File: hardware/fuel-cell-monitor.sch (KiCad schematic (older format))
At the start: 6 parts

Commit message: Upgraded version
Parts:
- added D?: Indicator, symbol LED
- added R?: 1k, symbol R
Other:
- moved on the sheet: SW?
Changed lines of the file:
@@
 LIBS:valves
 LIBS:arduino
+LIBS:fuel-cell-monitor-cache
 EELAYER 25 0
 EELAYER END
@@
 L SW_PUSH SW?
 U 1 1 582C96D8
-P 5300 3250
-F 0 "SW?" H 5450 3360 50  0000 C CNN
-F 1 "Write_control" H 5300 3170 50  0000 C CNN
-F 2 "" H 5300 3250 50  0000 C CNN
-F 3 "" H 5300 3250 50  0000 C CNN
-	1    5300 3250
+P 5250 3250
+F 0 "SW?" H 5400 3360 50  0000 C CNN
+F 1 "Write_control" H 5250 3170 50  0000 C CNN
+F 2 "" H 5250 3250 50  0000 C CNN
+F 3 "" H 5250 3250 50  0000 C CNN
+	1    5250 3250
 	0    1    1    0
 $EndComp
@@
 L GND #PWR?
 U 1 1 582C975D
-P 5300 3550
-F 0 "#PWR?" H 5300 3300 50  0001 C CNN
-F 1 "GND" H 5300 3400 50  0000 C CNN
-F 2 "" H 5300 3550 50  0000 C CNN
-F 3 "" H 5300 3550 50  0000 C CNN
-	1    5300 3550
+P 5250 3550
+F 0 "#PWR?" H 5250 3300 50  0001 C CNN
+F 1 "GND" H 5250 3400 50  0000 C CNN
+F 2 "" H 5250 3550 50  0000 C CNN
+F 3 "" H 5250 3550 50  0000 C CNN
+	1    5250 3550
 	1    0    0    -1
 $EndComp
 Wire Wire Line
-	5300 2950 4550 2950
+	5250 2950 4550 2950
+$Comp
+L LED D?
+U 1 1 582DD429
+P 5050 2650
+F 0 "D?" H 5050 2750 50  0000 C CNN
+F 1 "Indicator" H 5050 2550 50  0000 C CNN
+F 2 "" H 5050 2650 50  0000 C CNN
+F 3 "" H 5050 2650 50  0000 C CNN
+	1    5050 2650
+	-1   0    0    1
+$EndComp
+$Comp
+L R R?
+U 1 1 582DD478
+P 4700 2650
+F 0 "R?" V 4780 2650 50  0000 C CNN
+F 1 "1k" V 4700 2650 50  0000 C CNN
+F 2 "" V 4630 2650 50  0000 C CNN
+F 3 "" H 4700 2650 50  0000 C CNN
+	1    4700 2650
+	0    1    1    0
+$EndComp
+$Comp
+L GND #PWR?
+U 1 1 582DD4F9
+P 5250 2650
+F 0 "#PWR?" H 5250 2400 50  0001 C CNN
+F 1 "GND" H 5250 2500 50  0000 C CNN
+F 2 "" H 5250 2650 50  0000 C CNN
+F 3 "" H 5250 2650 50  0000 C CNN
+	1    5250 2650
+	1    0    0    -1
+$EndComp
 $EndSCHEMATC

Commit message: Add multiple things to schematic
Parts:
- removed R?: 470, symbol R
- removed U?: arduino_mini, DIL20, symbol arduino_mini
- added ARDUINO?: ARDUINO_NANO, symbol ARDUINO_NANO
- added D?: LED, symbol LED
- added D?: D_Schottky, symbol D_Schottky
- added M?: Solution pump, symbol DC_motor
- added M?: Air pump, symbol DC_motor
- added P?: Sense check, symbol CONN_01X02
- added P?: Light level sensor, symbol CONN_01X03
- added P?: Opacity sensor, symbol CONN_01X03
- added Q?: TEPT5600, symbol OPTO_NPN
- added Q?: TEPT5700, symbol OPTO_NPN
- added Q?: Q_NMOS_GDS, symbol Q_NMOS_GDS
- added R?: 10 k, symbol RVAR
- added R?: 1 k, symbol RVAR
- added R? (x2): 1 k, symbol R
- added R? (x2): 100, symbol R
- added R?: 1 M, symbol R
- added U?: LM35, symbol LM35
- P?: value Power_in -> Power in
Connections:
- net labels added: +12V, +5V
- wire segments 7 -> 33
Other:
- note added: "Light level sensor\n"
- note added: "Opacity sensor"
- moved on the sheet: D?, P?, R?, SW?

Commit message: Add missing parts to schematics
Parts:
- removed D?: Indicator, symbol LED
- removed D?: LED, symbol LED
- removed P?: Light level sensor, symbol CONN_01X03
- removed P?: Opacity sensor, symbol CONN_01X03
- removed Q?: TEPT5600, symbol OPTO_NPN
- removed Q?: TEPT5700, symbol OPTO_NPN
- removed R?: 1k, symbol R
- removed R? (x2): 1 k, symbol R
- removed R?: 100, symbol R
- added D?: Indicator, symbol LED
- added DS?: NHD-12232AZ, NHD-12232AZ, symbol NHD-12232AZ
- added R?: R, symbol R
- added RV?: 10 kA, symbol POT
- added S?: Light_level_sensor, symbol Light_level_sensor
- added S?: Opacity_sensor, symbol Opacity_sensor
- U?: value LM35 -> Temperature sensor
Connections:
- wire segments 33 -> 72
- no-connect marks 0 -> 6
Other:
- note removed: "Light level sensor\n"
- note removed: "Opacity sensor"
- moved on the sheet: ARDUINO?, D?, M?, P?, Q?, R?, SW?, U?

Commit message: Fix problems found with KiCad electrical rules check
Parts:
- gave numbers to parts that had none: 21
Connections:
- net +12V: now also ARDUINO1.30 (VIN), M2.2, P1.1 (P1)
- net at Q1.1 (G), R2.2: now also R1.1
- no-connect marks 6 -> 7
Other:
- moved on the sheet: P1, R1, R2

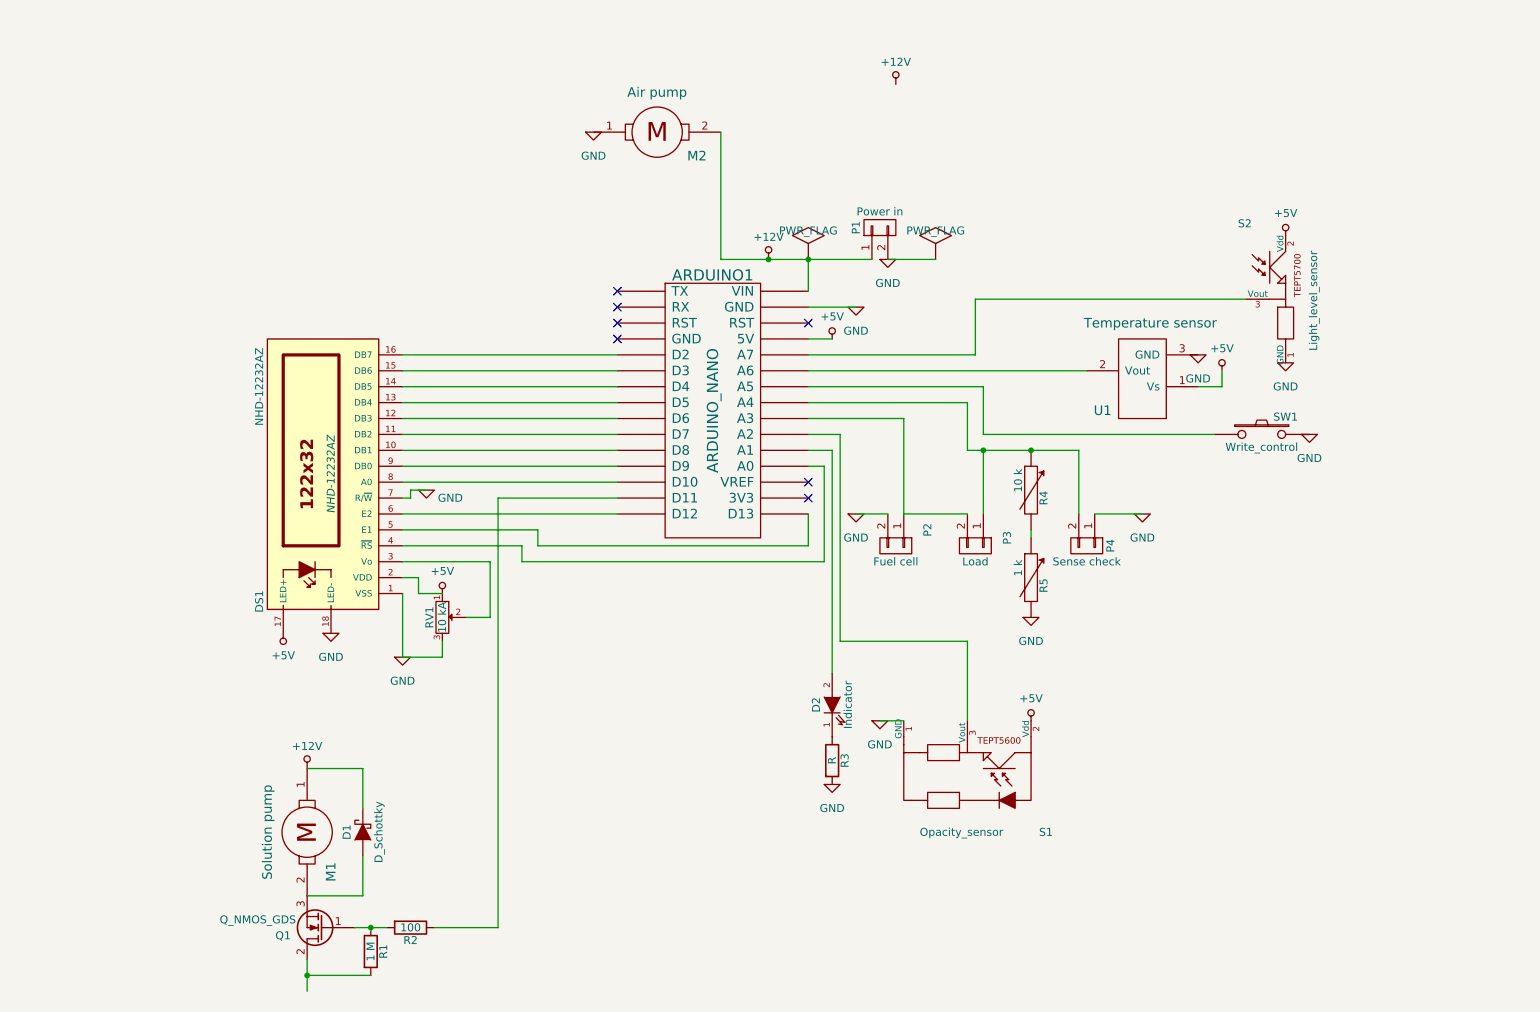
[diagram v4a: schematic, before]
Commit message: Fix remaining small things with the printed circuit board
This included making the default trace 0.40 mm wide just be sure
and fixing trimmer and potetiometer footprints.
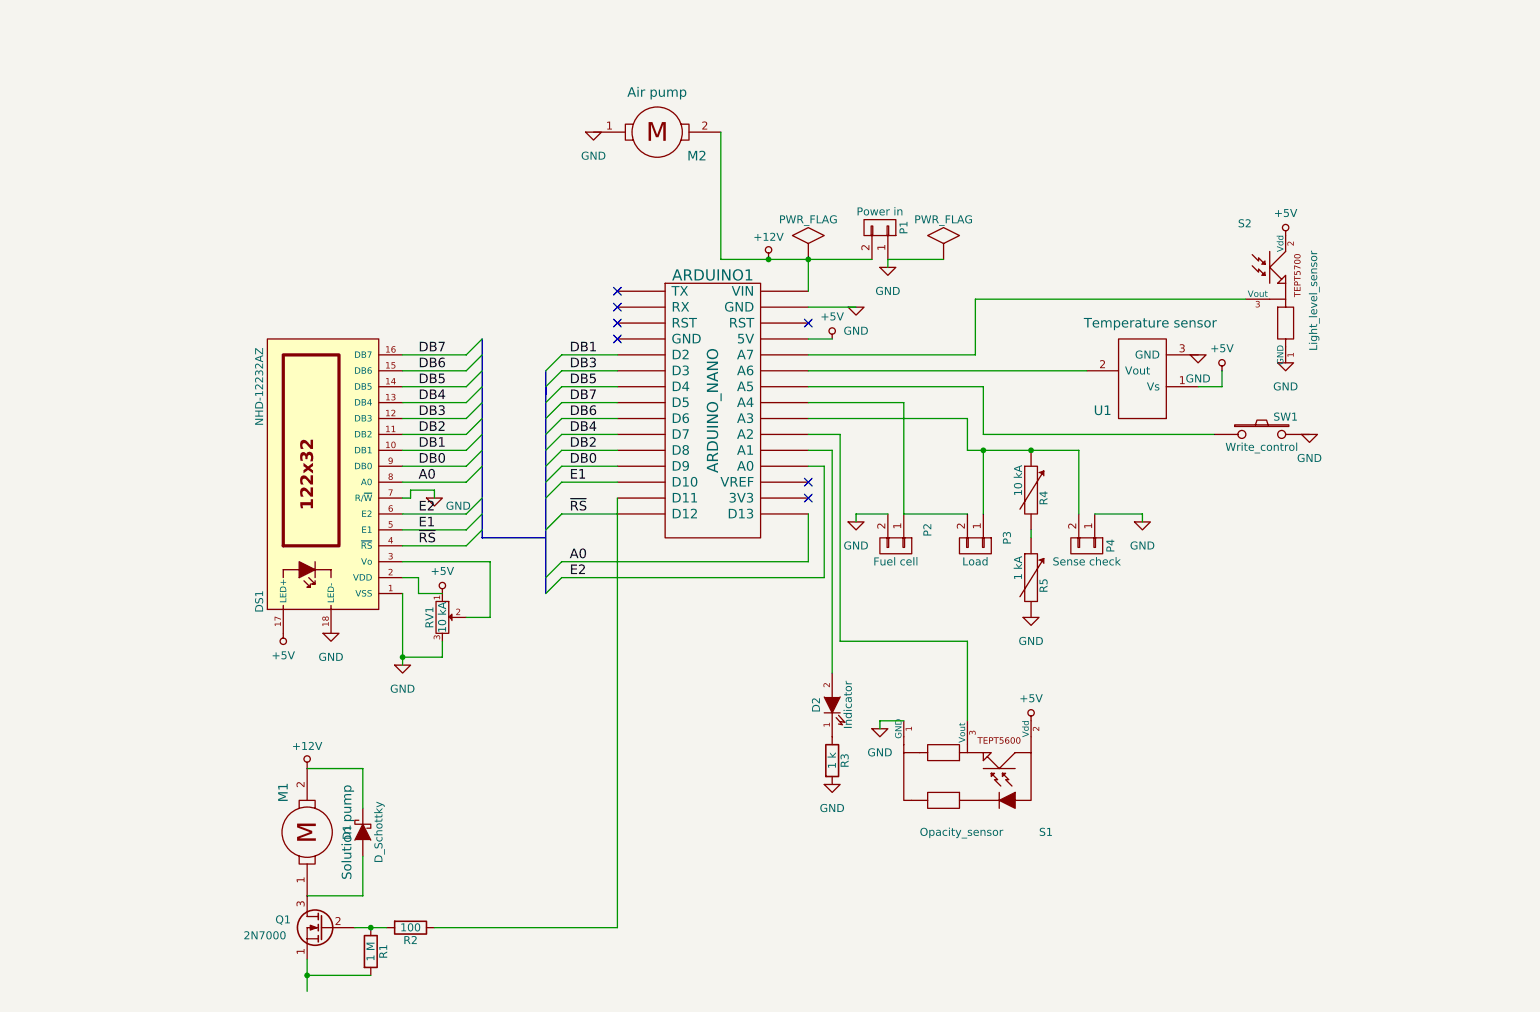
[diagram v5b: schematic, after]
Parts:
- removed Q1: Q_NMOS_GDS, symbol Q_NMOS_GDS
- added Q1: 2N7000, TO_SOT_Packages_THT:TO-92_Inline_Wide, symbol Q_NMOS_SGD
- ARDUINO1: footprint (none) -> w_conn_misc:arduino_nano_header
- D1: footprint (none) -> Diodes_ThroughHole:Diode_DO-35_SOD27_Horizontal_RM10
- D2: footprint (none) -> LEDs:LED-5MM
- DS1: footprint NHD-12232AZ -> Connect:IDC_Header_Straight_20pins
- M1, M2, P1, P2, P3: footprint (none) -> oturpe-kicad-modules:Big_green_chocolate_1x2
- P4: footprint (none) -> Connect:PINHEAD1-2
- R1, R2: footprint (none) -> Resistors_ThroughHole:Resistor_Horizontal_RM10mm
- R3: value R -> 1 k; footprint (none) -> Resistors_ThroughHole:Resistor_Horizontal_RM10mm
- R4: value 10 k -> 10 kA; footprint (none) -> Potentiometers:Potentiometer_Triwood_RM-065
- R5: value 1 k -> 1 kA; footprint (none) -> Potentiometers:Potentiometer_Triwood_RM-065
- RV1: footprint (none) -> Potentiometers:Potentiometer_Triwood_RM-065
- S1, S2, U1: footprint (none) -> oturpe-kicad-modules:Big_green_chocolate_1x3
- SW1: footprint (none) -> oturpe-kicad-modules:SW_PUSH_6mmx6mm
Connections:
- net +12V: now also M1.2, P1.2 (P2); no longer M1.1, P1.1 (P1)
- net GND: now also P1.1 (P1); no longer P1.2 (P2)
- net at P3.1 (P1), P4.2 (P2), R4.1: now also ARDUINO1.22 (A3); no longer ARDUINO1.23 (A4)
- net at P2.1 (P1), P3.2 (P2): now also ARDUINO1.23 (A4); no longer ARDUINO1.22 (A3)
- net DB2: now reaches DS1.11 (DB2)
- net DB2: now also ARDUINO1.11 (D8); no longer ARDUINO1.10 (D7)
- net DB1: now reaches DS1.10 (DB1)
- net DB1: now also ARDUINO1.5 (D2); no longer ARDUINO1.11 (D8)
- net DB0: now reaches ARDUINO1.12 (D9), DS1.9 (DB0)
- net A0: now reaches DS1.8 (A0)
- net A0: now also ARDUINO1.16 (D13); no longer ARDUINO1.13 (D10)
- net E2: now reaches DS1.6 (E2)
- net E2: now also ARDUINO1.19 (A0); no longer ARDUINO1.15 (D12)
- net E1: now reaches DS1.5 (E1)
- net E1: now also ARDUINO1.13 (D10); no longer ARDUINO1.16 (D13)
- net ~RS: now reaches DS1.4 (~RS)
- net ~RS: now also ARDUINO1.15 (D12); no longer ARDUINO1.19 (A0)
- net DB7: now reaches DS1.16 (DB7)
- net DB7: now also ARDUINO1.8 (D5); no longer ARDUINO1.5 (D2)
- net DB3: now reaches ARDUINO1.6 (D3)
- net DB3: now also DS1.12 (DB3); no longer DS1.15 (DB6)
- net DB5: now reaches ARDUINO1.7 (D4), DS1.14 (DB5)
- net DB4: now reaches DS1.13 (DB4)
- net DB4: now also ARDUINO1.10 (D7); no longer ARDUINO1.8 (D5)
- net DB6: now reaches ARDUINO1.9 (D6)
- net DB6: now also DS1.15 (DB6); no longer DS1.12 (DB3)
- net at R1.1, R2.2: now also Q1.2 (G)
- net at R1.2: now also Q1.1 (S)
- net at D1.2 (A): now also M1.1, Q1.3 (D); no longer M1.2

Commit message: Fix potentiometer and trimmer footprint
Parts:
- R4, R5, RV1: footprint Potentiometers:Potentiometer_Triwood_RM-065 -> oturpe-kicad-modules:Trimmer_ACP_*V10
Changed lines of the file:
@@
 F 0 "R4" V 8330 3500 50  0000 C CNN
 F 1 "10 kA" V 8170 3610 50  0000 C CNN
-F 2 "Potentiometers:Potentiometer_Triwood_RM-065" H 8250 3550 50  0001 C CNN
+F 2 "oturpe-kicad-modules:Trimmer_ACP_*V10" H 8250 3550 50  0001 C CNN
 F 3 "" H 8250 3550 50  0000 C CNN
 	1    8250 3550
@@
 F 0 "R5" V 8330 4050 50  0000 C CNN
 F 1 "1 kA" V 8170 4160 50  0000 C CNN
-F 2 "Potentiometers:Potentiometer_Triwood_RM-065" H 8250 4100 50  0001 C CNN
+F 2 "oturpe-kicad-modules:Trimmer_ACP_*V10" H 8250 4100 50  0001 C CNN
 F 3 "" H 8250 4100 50  0000 C CNN
 	1    8250 4100
@@
 F 0 "RV1" H 4550 4270 50  0000 C CNN
 F 1 "10 kA" H 4550 4350 50  0000 C CNN
-F 2 "Potentiometers:Potentiometer_Triwood_RM-065" H 4550 4350 50  0001 C CNN
+F 2 "oturpe-kicad-modules:Trimmer_ACP_*V10" H 4550 4350 50  0001 C CNN
 F 3 "" H 4550 4350 50  0000 C CNN
 	1    4550 4350

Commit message: Final fixes before ordering pcbs.
Most notably solution pump driver mosfet had to be changed. The earlier
specified type did not work.
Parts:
- Q1: value 2N7000 -> IRLLU024N; footprint TO_SOT_Packages_THT:TO-92_Inline_Wide -> TO_SOT_Packages_THT:TO-251AA; symbol Q_NMOS_SGD -> Q_NMOS_GDS
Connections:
- net GND: now also Q1.3 (S), R1.2
- net at D1.2 (A), M1.1: now also Q1.2 (D); no longer Q1.3 (D)
- net at R1.1, R2.2: now also Q1.1 (G); no longer Q1.2 (G)
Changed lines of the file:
@@
 $EndComp
 $Comp
-L Q_NMOS_SGD Q1
+L Q_NMOS_GDS Q1
 U 1 1 5837F87A
 P 3800 6300
 F 0 "Q1" H 4100 6350 50  0000 R CNN
-F 1 "2N7000" H 4300 6250 50  0000 R CNN
-F 2 "TO_SOT_Packages_THT:TO-92_Inline_Wide" H 4000 6400 50  0001 C CNN
+F 1 "IRLLU024N" H 4400 6250 50  0000 R CNN
+F 2 "TO_SOT_Packages_THT:TO-251AA" H 4000 6400 50  0001 C CNN
 F 3 "" H 3800 6300 50  0000 C CNN
 	1    3800 6300
@@
 Wire Wire Line
 	7850 3100 7850 3300
+$Comp
+L GND #PWR025
+U 1 1 583DA334
+P 3700 6700
+F 0 "#PWR025" H 3700 6700 30  0001 C CNN
+F 1 "GND" H 3700 6630 30  0001 C CNN
+F 2 "" H 3700 6700 60  0001 C CNN
+F 3 "" H 3700 6700 60  0001 C CNN
+	1    3700 6700
+	1    0    0    -1
+$EndComp
 $EndSCHEMATC
